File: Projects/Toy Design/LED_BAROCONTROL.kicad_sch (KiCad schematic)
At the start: 39 parts, among them U12 74HC595, U13 74HC595, U14 74HC595, U15 74HC595, U16 74HC595, U17 74HC595

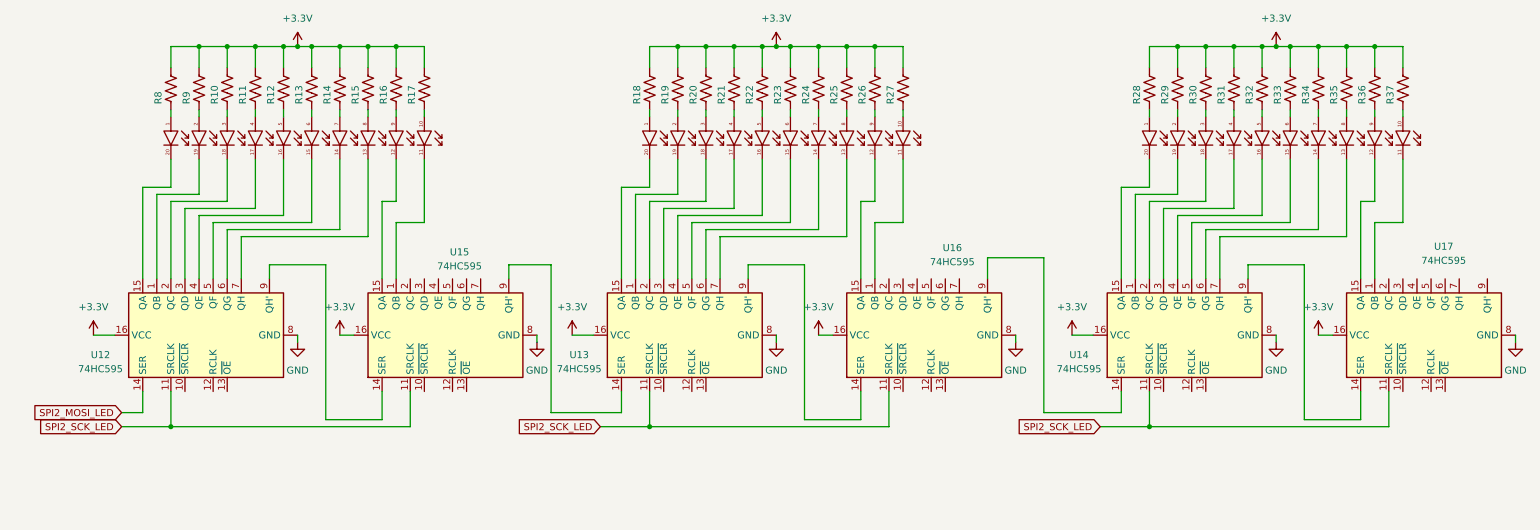
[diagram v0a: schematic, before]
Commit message: started pcb post led bar
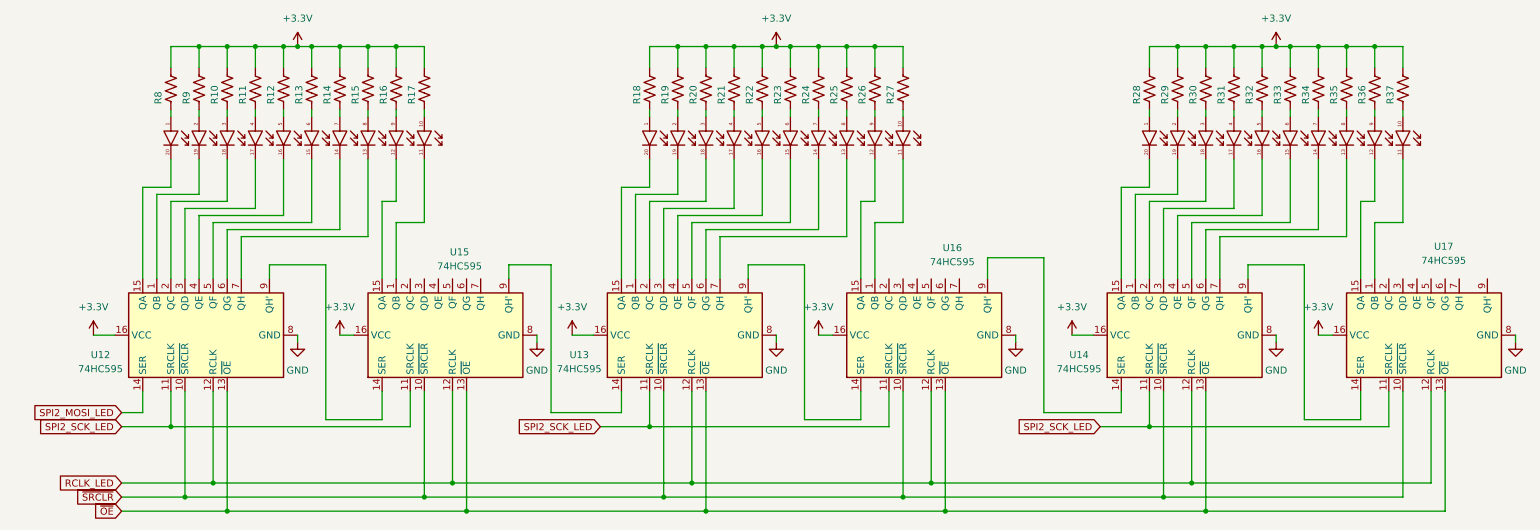
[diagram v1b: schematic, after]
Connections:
- net ~{SRCLR}: now reaches U17.10 (~{SRCLR})
- net ~{SRCLR}: now also U12.10 (~{SRCLR}), U13.10 (~{SRCLR}), U14.10 (~{SRCLR}), U15.10 (~{SRCLR}), U16.10 (~{SRCLR})
- net RCLK_LED: now reaches U17.12 (RCLK)
- net RCLK_LED: now also U12.12 (RCLK), U13.12 (RCLK), U14.12 (RCLK), U15.12 (RCLK), U16.12 (RCLK)
- net ~{OE}: now reaches U17.13 (~{OE})
- net ~{OE}: now also U12.13 (~{OE}), U13.13 (~{OE}), U14.13 (~{OE}), U15.13 (~{OE}), U16.13 (~{OE})
